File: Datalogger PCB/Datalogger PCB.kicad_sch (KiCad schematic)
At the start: 48 parts, among them J1 Conn_01x02_Pin, M1 Motor_Servo, M2 Motor_Servo, M3 Motor_Servo, M4 Motor_Servo, U1 Teensy4.1, U2 BNO055, U3 LPS25HB, U4 AMS1117-5.0, U6 VN5E160STR-E, U7 VN5E160STR-E, U8 VN5E160STR-E, U9 VN5E160STR-E

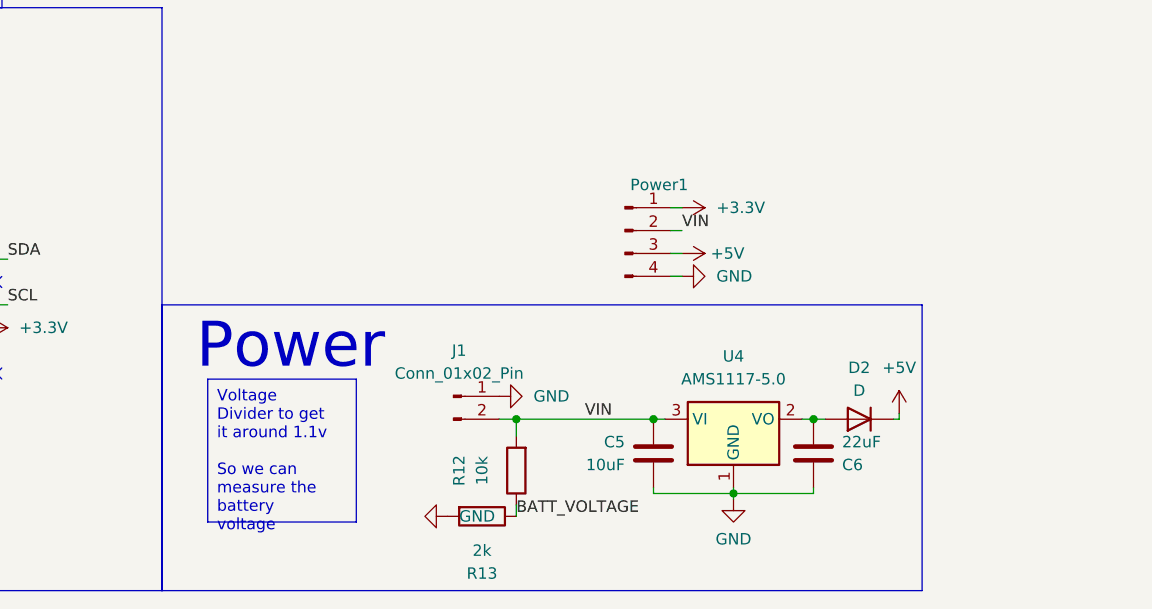
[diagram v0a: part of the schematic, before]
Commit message: Removed Diode and replaced with jumper
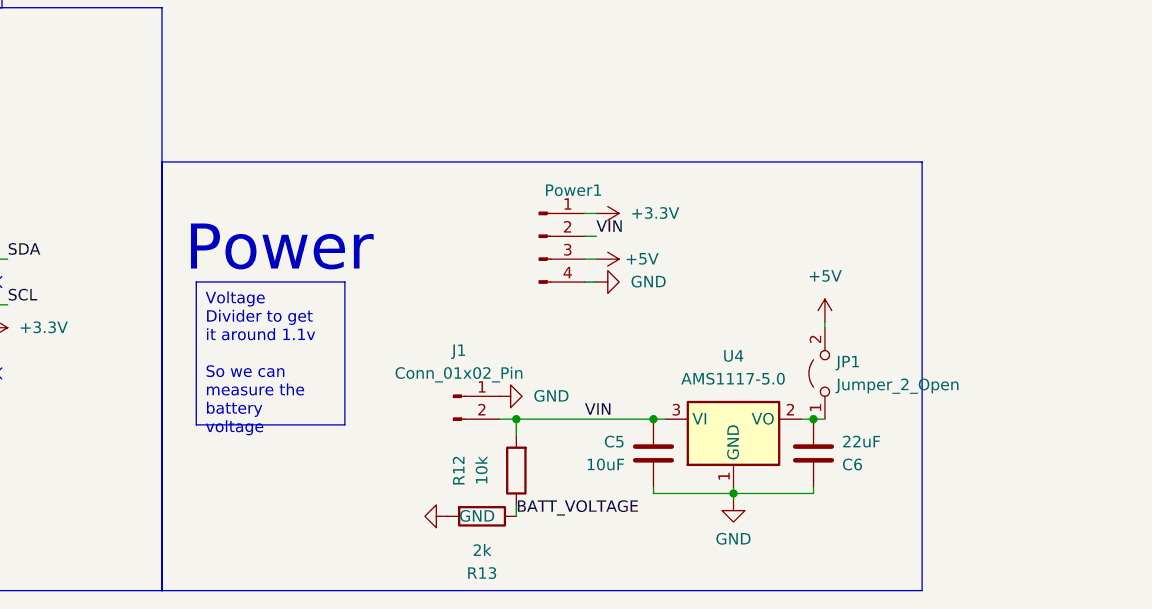
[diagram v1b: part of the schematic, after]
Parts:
- removed D2: D, Diode_SMD:D_0603_1608Metric_Pad1.05x0.95mm_HandSolder, symbol Device:D
- added JP1: Jumper_2_Open, Connector_PinHeader_2.00mm:PinHeader_1x02_P2.00mm_Vertical, symbol Jumper:Jumper_2_Open
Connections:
- net +5V: now also JP1.2 (B)
- net at C6.2, U4.2 (VO): now also JP1.1 (A)
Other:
- moved on the sheet: Power1
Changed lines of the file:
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@@
     (stroke (width 0) (type default))
   )
-  (wire (pts (xy 233.045 184.15) (xy 233.045 184.785))
+  (wire (pts (xy 224.79 173.99) (xy 224.79 174.625))
     (stroke (width 0) (type default))
   )
@@
     (stroke (width 0) (type default))
   )
-  (wire (pts (xy 233.045 184.785) (xy 232.41 184.785))
-    (stroke (width 0) (type default))
-  )
   (wire (pts (xy 303.53 41.275) (xy 304.8 41.275))
     (stroke (width 0) (type default))
@@
     (stroke (width 0) (type default))
   )
-  (wire (pts (xy 208.915 168.91) (xy 207.645 168.91))
+  (wire (pts (xy 199.39 169.545) (xy 198.12 169.545))
     (stroke (width 0) (type default))
   )
@@
     (stroke (width 0) (type default))
   )
-  (wire (pts (xy 208.915 163.83) (xy 207.645 163.83))
+  (wire (pts (xy 199.39 164.465) (xy 198.12 164.465))
     (stroke (width 0) (type default))
   )
@@
     (stroke (width 0) (type default))
   )
-  (wire (pts (xy 208.915 161.29) (xy 207.645 161.29))
+  (wire (pts (xy 199.39 161.925) (xy 198.12 161.925))
     (stroke (width 0) (type default))
   )
@@
     (stroke (width 0) (type default))
   )
-  (wire (pts (xy 208.915 166.37) (xy 207.645 166.37))
+  (wire (pts (xy 199.39 167.005) (xy 198.12 167.005))
     (stroke (width 0) (type default))
   )
@@
     (fill (type none))
   )
-  (rectangle (start 151.13 172.085) (end 235.585 203.835)
+  (rectangle (start 151.13 156.21) (end 235.585 203.835)
     (stroke (width 0) (type default))
     (fill (type none))
@@
   )
   (text_box "Voltage Divider to get it around 1.1v\n\nSo we can measure the battery voltage"
-    (at 156.21 180.34 0) (size 16.51 15.875)
+    (at 154.94 169.545 0) (size 16.51 15.875)
     (stroke (width 0) (type default))
     (fill (type none))
@@
     (effects (font (size 5 5)) (justify left bottom))
   )
-  (text "Power" (at 154.94 179.705 0)
+  (text "Power" (at 153.67 168.91 0)
     (effects (font (size 5 5)) (justify left bottom))
   )
@@
     (effects (font (size 1.27 1.27)) (justify left bottom))
   )
-  (label "VIN" (at 208.915 163.83 0) (fields_autoplaced)
+  (label "VIN" (at 199.39 164.465 0) (fields_autoplaced)
     (effects (font (size 1.27 1.27)) (justify left bottom))
   )
@@
     )
   )
-  (symbol (lib_id "power:+5V") (at 233.045 184.15 0) (unit 1)
+  (symbol (lib_id "power:+5V") (at 224.79 173.99 0) (unit 1)
     (in_bom yes) (on_board yes) (dnp no) (fields_autoplaced)
-    (property "Reference" "#PWR039" (at 233.045 187.96 0)
+    (property "Reference" "#PWR039" (at 224.79 177.8 0)
       (effects (font (size 1.27 1.27)) hide)
     )
-    (property "Value" "+5V" (at 233.045 179.07 0)
+    (property "Value" "+5V" (at 224.79 168.91 0)
       (effects (font (size 1.27 1.27)))
     )
-    (property "Footprint" "" (at 233.045 184.15 0)
+    (property "Footprint" "" (at 224.79 173.99 0)
       (effects (font (size 1.27 1.27)) hide)
     )
-    (property "Datasheet" "" (at 233.045 184.15 0)
+    (property "Datasheet" "" (at 224.79 173.99 0)
       (effects (font (size 1.27 1.27)) hide)
     )
@@
     )
   )
-  (symbol (lib_id "Device:D") (at 228.6 184.785 180) (unit 1)
-    (in_bom yes) (on_board yes) (dnp no) (fields_autoplaced)
-    (property "Reference" "D2" (at 228.6 179.07 0)
-      (effects (font (size 1.27 1.27)))
-    )
-    (property "Value" "D" (at 228.6 181.61 0)
-      (effects (font (size 1.27 1.27)))
-    )
-    (property "Footprint" "Diode_SMD:D_0603_1608Metric_Pad1.05x0.95mm_HandSolder" (at 228.6 184.785 0)
-      (effects (font (size 1.27 1.27)) hide)
-    )
-    (property "Datasheet" "~" (at 228.6 184.785 0)
-      (effects (font (size 1.27 1.27)) hide)
-    )
-    (property "Sim.Device" "D" (at 228.6 184.785 0)
-      (effects (font (size 1.27 1.27)) hide)
-    )
-    (property "Sim.Pins" "1=K 2=A" (at 228.6 184.785 0)
-      (effects (font (size 1.27 1.27)) hide)
-    )
-    (pin "1")
-    (pin "2")
-    (instances
-      (project "Datalogger PCB"
-        (path "/a3bc5533-d6ac-45b5-a7d9-fc1b12646794"
-          (reference "D2") (unit 1)
-        )
-      )
-    )
-  )
   (symbol (lib_id "power:+3.3V") (at 313.69 158.75 90) (unit 1)
     (in_bom yes) (on_board yes) (dnp no) (fields_autoplaced)
@@
     )
   )
-  (symbol (lib_id "power:+5V") (at 208.915 166.37 270) (unit 1)
+  (symbol (lib_id "power:+5V") (at 199.39 167.005 270) (unit 1)
     (in_bom yes) (on_board yes) (dnp no) (fields_autoplaced)
-    (property "Reference" "#PWR050" (at 205.105 166.37 0)
+    (property "Reference" "#PWR050" (at 195.58 167.005 0)
       (effects (font (size 1.27 1.27)) hide)
     )
-    (property "Value" "+5V" (at 212.09 166.37 90)
+    (property "Value" "+5V" (at 202.565 167.005 90)
       (effects (font (size 1.27 1.27)) (justify left))
     )
-    (property "Footprint" "" (at 208.915 166.37 0)
+    (property "Footprint" "" (at 199.39 167.005 0)
       (effects (font (size 1.27 1.27)) hide)
     )
-    (property "Datasheet" "" (at 208.915 166.37 0)
+    (property "Datasheet" "" (at 199.39 167.005 0)
       (effects (font (size 1.27 1.27)) hide)
     )
@@
     )
   )
-  (symbol (lib_id "power:+3.3V") (at 208.915 161.29 270) (unit 1)
+  (symbol (lib_id "power:+3.3V") (at 199.39 161.925 270) (unit 1)
     (in_bom yes) (on_board yes) (dnp no) (fields_autoplaced)
-    (property "Reference" "#PWR051" (at 205.105 161.29 0)
+    (property "Reference" "#PWR051" (at 195.58 161.925 0)
       (effects (font (size 1.27 1.27)) hide)
     )
-    (property "Value" "+3.3V" (at 212.725 161.29 90)
+    (property "Value" "+3.3V" (at 203.2 161.925 90)
       (effects (font (size 1.27 1.27)) (justify left))
     )
-    (property "Footprint" "" (at 208.915 161.29 0)
+    (property "Footprint" "" (at 199.39 161.925 0)
       (effects (font (size 1.27 1.27)) hide)
     )
-    (property "Datasheet" "" (at 208.915 161.29 0)
+    (property "Datasheet" "" (at 199.39 161.925 0)
       (effects (font (size 1.27 1.27)) hide)
     )
@@
     )
   )
+  (symbol (lib_id "Jumper:Jumper_2_Open") (at 224.79 179.705 90) (unit 1)
+    (in_bom yes) (on_board yes) (dnp no) (fields_autoplaced)
+    (property "Reference" "JP1" (at 226.06 178.435 90)
+      (effects (font (size 1.27 1.27)) (justify right))
+    )
+    (property "Value" "Jumper_2_Open" (at 226.06 180.975 90)
+      (effects (font (size 1.27 1.27)) (justify right))
+    )
+    (property "Footprint" "Connector_PinHeader_2.00mm:PinHeader_1x02_P2.00mm_Vertical" (at 224.79 179.705 0)
+      (effects (font (size 1.27 1.27)) hide)
+    )
+    (property "Datasheet" "~" (at 224.79 179.705 0)
+      (effects (font (size 1.27 1.27)) hide)
+    )
+    (pin "2")
+    (pin "1")
+    (instances
+      (project "Datalogger PCB"
+        (path "/a3bc5533-d6ac-45b5-a7d9-fc1b12646794"
+          (reference "JP1") (unit 1)
+        )
+      )
+    )
+  )
   (symbol (lib_id "Sensor_Motion:BNO055") (at 48.26 173.99 0) (unit 1)
     (in_bom yes) (on_board yes) (dnp no) (fields_autoplaced)
@@
     )
   )
-  (symbol (lib_id "power:GND") (at 208.915 168.91 90) (unit 1)
+  (symbol (lib_id "power:GND") (at 199.39 169.545 90) (unit 1)
     (in_bom yes) (on_board yes) (dnp no) (fields_autoplaced)
-    (property "Reference" "#PWR049" (at 215.265 168.91 0)
+    (property "Reference" "#PWR049" (at 205.74 169.545 0)
       (effects (font (size 1.27 1.27)) hide)
     )
-    (property "Value" "GND" (at 212.725 168.91 90)
+    (property "Value" "GND" (at 203.2 169.545 90)
       (effects (font (size 1.27 1.27)) (justify right))
     )
-    (property "Footprint" "" (at 208.915 168.91 0)
+    (property "Footprint" "" (at 199.39 169.545 0)
       (effects (font (size 1.27 1.27)) hide)
     )
-    (property "Datasheet" "" (at 208.915 168.91 0)
+    (property "Datasheet" "" (at 199.39 169.545 0)
       (effects (font (size 1.27 1.27)) hide)
     )
@@
     )
   )
-  (symbol (lib_id "Connector:Conn_01x04_Pin") (at 202.565 163.83 0) (unit 1)
+  (symbol (lib_id "Connector:Conn_01x04_Pin") (at 193.04 164.465 0) (unit 1)
     (in_bom yes) (on_board yes) (dnp no)
-    (property "Reference" "Power1" (at 206.375 158.75 0)
+    (property "Reference" "Power1" (at 196.85 159.385 0)
       (effects (font (size 1.27 1.27)))
     )
-    (property "Value" "Conn_01x04_Pin" (at 203.2 159.385 0)
+    (property "Value" "Conn_01x04_Pin" (at 193.675 160.02 0)
       (effects (font (size 1.27 1.27)) hide)
     )
-    (property "Footprint" "Connector_PinSocket_2.54mm:PinSocket_1x04_P2.54mm_Vertical" (at 202.565 163.83 0)
+    (property "Footprint" "Connector_PinSocket_2.54mm:PinSocket_1x04_P2.54mm_Vertical" (at 193.04 164.465 0)
       (effects (font (size 1.27 1.27)) hide)
     )
-    (property "Datasheet" "~" (at 202.565 163.83 0)
+    (property "Datasheet" "~" (at 193.04 164.465 0)
       (effects (font (size 1.27 1.27)) hide)
     )

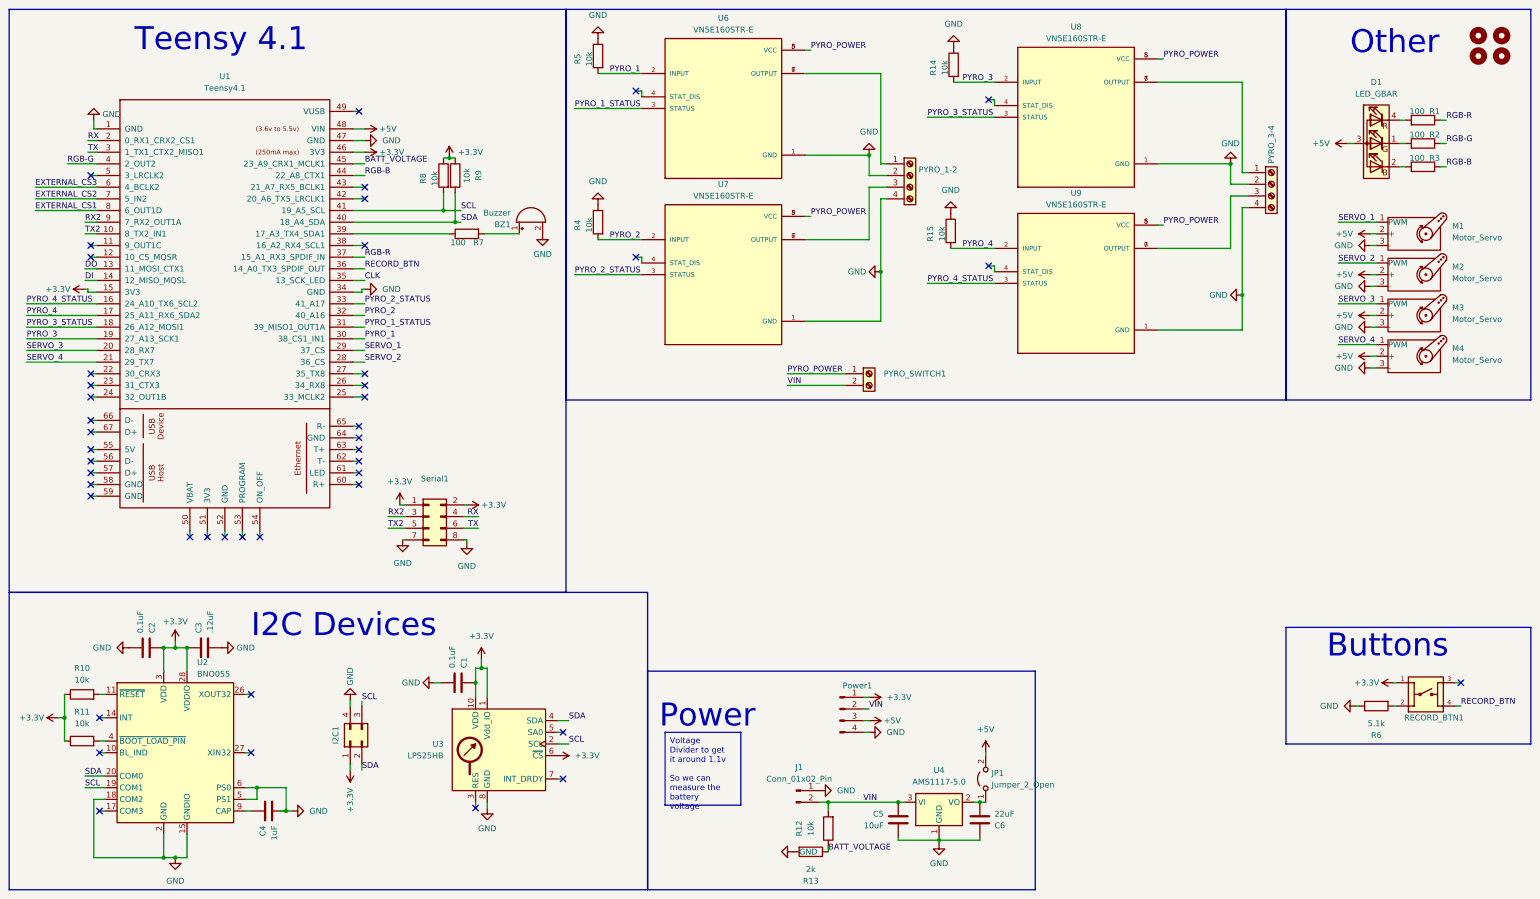
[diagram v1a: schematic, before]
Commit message: Added pyro armed
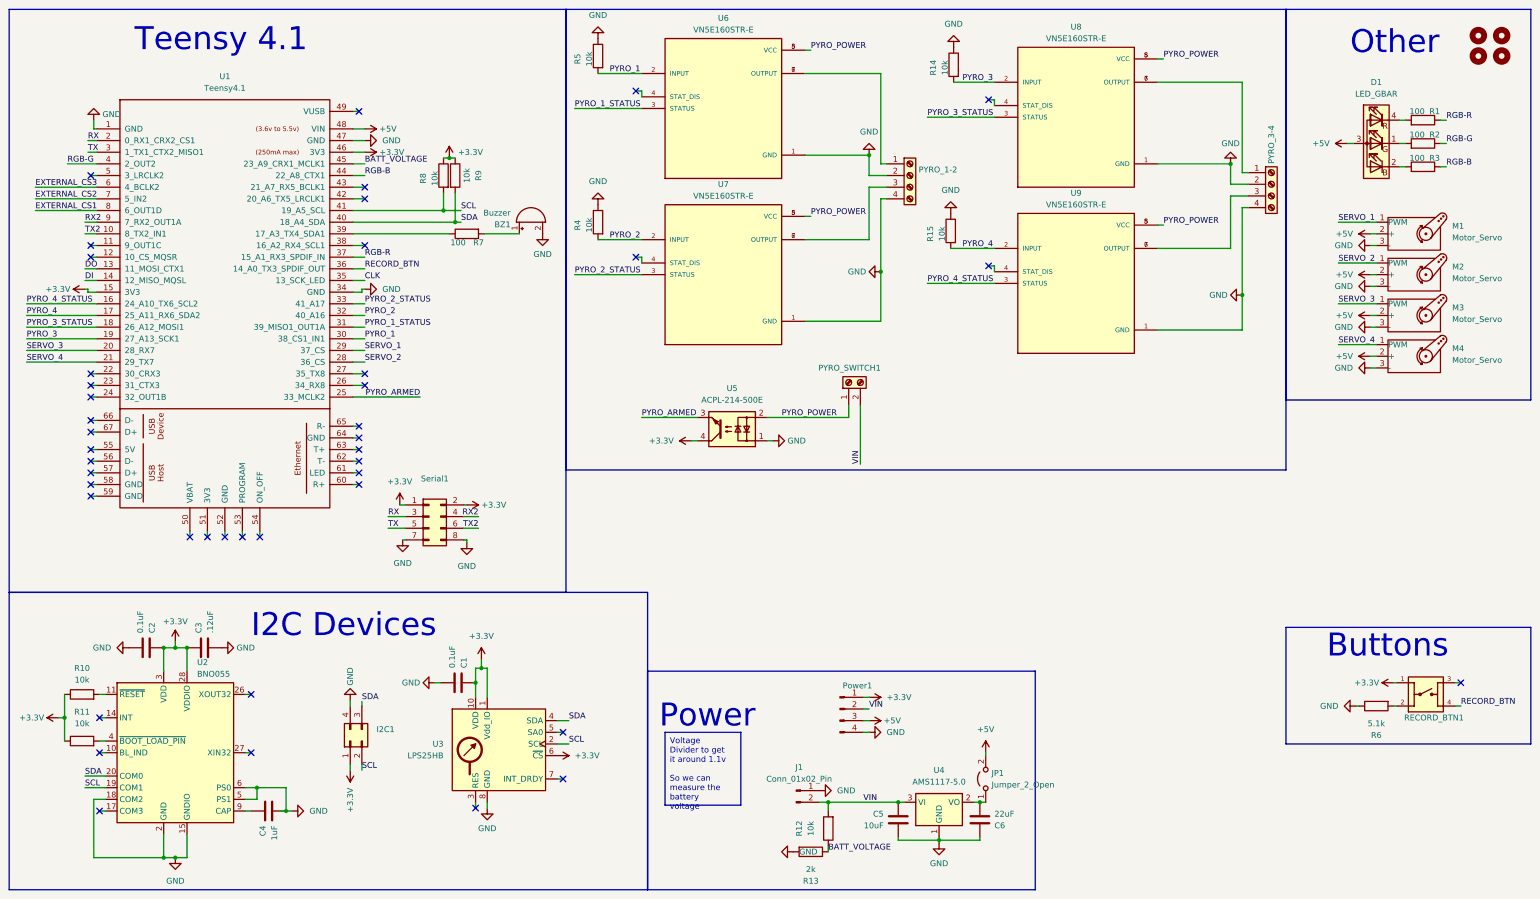
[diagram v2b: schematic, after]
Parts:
- added U5: ACPL-214-500E, Package_SO:SOP-4_4.4x2.6mm_P1.27mm, symbol Isolator:ACPL-214-500E
- I2C1: footprint Connector_PinSocket_2.54mm:PinSocket_2x02_P2.54mm_Vertical -> Connector_PinHeader_2.54mm:PinHeader_2x02_P2.54mm_Vertical
- Power1: footprint Connector_PinSocket_2.54mm:PinSocket_1x04_P2.54mm_Vertical -> Connector_PinHeader_2.54mm:PinHeader_1x04_P2.54mm_Vertical
- Serial1: footprint Connector_PinSocket_2.54mm:PinSocket_2x04_P2.54mm_Vertical -> Connector_PinHeader_2.54mm:PinHeader_2x04_P2.54mm_Vertical
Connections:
- net +3.3V: now also U5.4
- net GND: now also U5.1
- net PYRO_POWER: now also U5.2
- net RX: now also Serial1.3 (Pin_3); no longer Serial1.4 (Pin_4)
- net RX2: now also Serial1.4 (Pin_4); no longer Serial1.3 (Pin_3)
- net SCL: now also I2C1.2 (Pin_2); no longer I2C1.3 (Pin_3)
- net SDA: now also I2C1.3 (Pin_3); no longer I2C1.2 (Pin_2)
- net TX: now also Serial1.5 (Pin_5); no longer Serial1.6 (Pin_6)
- net TX2: now also Serial1.6 (Pin_6); no longer Serial1.5 (Pin_5)
- net PYRO_ARMED: now reaches U1.25 (33_MCLK2)
- net PYRO_ARMED: now also U5.3
- no-connect marks 44 -> 43
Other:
- moved on the sheet: PYRO_SWITCH1
